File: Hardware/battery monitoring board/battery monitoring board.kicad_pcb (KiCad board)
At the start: 2 copper layers, 142 x 53.3 mm, 71 parts, among them J1 Conn_01x02, J10 Conn_01x02, J2 Conn_01x02, J3 S5B-XH-A, J4 Conn_01x02, J5 Conn_01x02, J6 Conn_01x02, J7 Conn_01x02, J8 Conn_01x02, J9 S5B-XH-A, K1 Relay_SPST-NO, Q1 PNP, Q2 PN2222A, U1 MAX31855KASA

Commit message: rearranged parts
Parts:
- moved J4 56.4 mm to (138.4, 61.6), turned to 90 degrees
- moved J3 48.6 mm to (145.7, 47.3), turned to 90 degrees
- moved J9 45.3 mm to (145.4, 30.5), turned to 90 degrees
- moved FB2 42.6 mm to (130.8, 67.7), turned to 180 degrees
- moved TP4 38.6 mm to (132.1, 61.6), turned to 0 degrees
- moved FB1 37.9 mm to (132.1, 60.6), turned to 90 degrees
- moved TP5 37.3 mm to (132.1, 59.6), turned to 0 degrees
- moved R3 35.6 mm to (135.8, 41.3), turned to -90 degrees
- moved TP6 32.1 mm to (128.6, 61.6), turned to 0 degrees
- moved TP9 31.6 mm to (119.7, 70.4), turned to 0 degrees
- moved C4 31.5 mm to (128.6, 60.9), turned to -90 degrees
- moved R4 31.1 mm to (132.3, 41.3), turned to 90 degrees
- moved TP7 30.5 mm to (128.6, 59.6), turned to 0 degrees
- moved R5 29.7 mm to (135.8, 45.4), turned to 90 degrees
- moved R2 29.6 mm to (135.7, 53.6), turned to -90 degrees
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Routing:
- net /voltage monitor/OUT1: track 51.1 -> 5.37 mm
- net /voltage monitor2/OUT1: track 49.5 -> 6.77 mm
- net /voltage monitor2/OUT4: track 38.0 -> 9.09 mm
- net Net-(A1-D4): track 27.4 -> 0.00 mm, vias 1 -> 0
- net /voltage monitor2/OUT3: track 36.1 -> 9.33 mm
- net /voltage monitor/OUT3: track 34.3 -> 8.59 mm
- net /voltage monitor/OUT2: track 33.9 -> 8.69 mm
- net /voltage monitor2/OUT2: track 34.1 -> 9.13 mm
- net /voltage monitor/OUT4: track 33.5 -> 8.76 mm
- net /leak sensor/LEAK_SIGNAL: track 39.7 -> 15.9 mm
- net /e-switch/MCU_OUTPUT: track 23.8 -> 0.00 mm, vias 2 -> 0
- net +3V3: track 74.1 -> 61.0 mm, vias 1 -> 0
- net /temp sensor/cs: track 16.4 -> 26.9 mm, vias 1 -> 0
- net /temp sensor/sck: track 26.1 -> 16.5 mm, vias 1 -> 0
- net +9V: track 102.9 -> 94.0 mm
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
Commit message: updated battery board pt.II
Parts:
- removed TP4, TP5, TP6, TP7: TestPoint, Library:Test Pads
- added 1: TestPoint, PCM_4ms_TestPoint:TestPoint_Pad_06, F.Cu at (115.8, 70.1)
- added 1: TestPoint, PCM_4ms_TestPoint:TestPoint_Pad_06, F.Cu at (115.3, 56.6)
- added C1: 10nF, Capacitor_SMD:C_0805_2012Metric_Pad1.18x1.45mm_HandSolder, F.Cu at (122.2, 74.2)
- added C8: 10nF, Capacitor_SMD:C_0805_2012Metric_Pad1.18x1.45mm_HandSolder, F.Cu at (121.9, 57.4)
- added D2: Green LED, Diode_SMD:D_0805_2012Metric_Pad1.15x1.40mm_HandSolder, F.Cu at (98.5, 43.4)
- added D8: LED, Diode_SMD:D_0805_2012Metric_Pad1.15x1.40mm_HandSolder, F.Cu at (138.4, 70.4)
- added R18: 360, Resistor_SMD:R_0805_2012Metric_Pad1.20x1.40mm_HandSolder, F.Cu at (141.5, 70.4)
- added R2: 150, Resistor_SMD:R_0805_2012Metric_Pad1.20x1.40mm_HandSolder, F.Cu at (103.4, 43.4)
- added U1: MCP3008, PCM_Package_SO_AKL:SOIC-16_3.9x9.9mm_P1.27mm, F.Cu at (109.9, 56.1)
- 2: renamed from TP16; footprint Library:Test Pads -> PCM_4ms_TestPoint:TestPoint_Pad_06
- 2: renamed from TP3; footprint Library:Test Pads -> PCM_4ms_TestPoint:TestPoint_Pad_06
- 3: renamed from TP15; footprint Library:Test Pads -> PCM_4ms_TestPoint:TestPoint_Pad_06
- 3: renamed from TP2; footprint Library:Test Pads -> PCM_4ms_TestPoint:TestPoint_Pad_06
- 4: renamed from TP14; footprint Library:Test Pads -> PCM_4ms_TestPoint:TestPoint_Pad_06
- 4: renamed from TP1; footprint Library:Test Pads -> PCM_4ms_TestPoint:TestPoint_Pad_06
- D7: renamed from D5; footprint Diode_SMD:D_0805_2012Metric_Pad1.15x1.40mm_HandSolder -> Diode_SMD:D_SMA
- J3, J9: footprint Library:JST_S5B-XH-A -> Connector_JST:JST_XH_B5B-XH-A_1x05_P2.50mm_Vertical
- J9: renamed from J10; footprint Library:JST_BM02B-GHS-TBT_LF__SN_ -> Library:DEANS
- Leak: renamed from TP11; footprint Library:Test Pads -> PCM_4ms_TestPoint:TestPoint_Pad_06; moved to F.Cu
- R1: value 147 -> 150
- R21: renamed from R22; value 11.5k -> 20.5k
- R24: renamed from R21; value 16.5k -> 11.5k
- R25: renamed from R18; value 19.6k -> 23.2k
- R5: renamed from R7; value 11.5k -> 20.5k
- R8: renamed from R6; value 16.5k -> 11.5k
- R9: renamed from R3; value 19.6k -> 23.2k
- TP10: renamed from TP9; footprint Library:Test Pads -> PCM_4ms_TestPoint:TestPoint_Pad_06
- TP13: renamed from TP12; footprint Library:Test Pads -> PCM_4ms_TestPoint:TestPoint_Pad_06; moved to F.Cu
- TP14: renamed from TP13; footprint Library:Test Pads -> PCM_4ms_TestPoint:TestPoint_Pad_06; moved to F.Cu
- TP9: renamed from TP8; footprint Library:Test Pads -> PCM_4ms_TestPoint:TestPoint_Pad_06; moved to F.Cu
- sck: renamed from TP10; footprint Library:Test Pads -> PCM_4ms_TestPoint:TestPoint_Pad_06
- moved R13 64.8 mm to (82.3, 85.9), turned to 90 degrees
- moved R14 64.0 mm to (83.1, 82.3), turned to 180 degrees
- moved Q1 63.9 mm to (82.8, 76.5)
- moved R15 63.9 mm to (82.8, 72.4)
- moved R16 63.9 mm to (82.8, 68.8)
- moved D6 63.8 mm to (82.8, 65.5)
- moved Leak 59.9 mm to (84.8, 62.2), turned to 0 degrees
- moved R1 51.8 mm to (88.1, 43.4), turned to 0 degrees
- moved C7 47.4 mm to (82.0, 90.4)
- moved TP9 41.3 mm to (111.0, 97.5), turned to 180 degrees
- moved D1 40.9 mm to (93.2, 43.4), turned to 0 degrees
- moved sck 36.2 mm to (103.6, 98.3)
- moved D4 29.4 mm to (109.0, 82.3), turned to 0 degrees
- moved J3 29.1 mm to (130.6, 72.2)
- moved J9 29.1 mm to (130.5, 55.5)
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- renumbered C8 to C10, C7 to C11, C3 to C2, C2 to C3, C1 to C4, C4 to C5, C5 to C6, C6 to C7, D2 to D4, D3 to D5, D4 to D6, R4 to R10, R9 to R11, R10 to R12, R11 to R13, R12 to R14, R13 to R15, R14 to R16, R15 to R17, R16 to R19, R17 to R20, R23 to R22, R20 to R23, R19 to R26, R2 to R4, R8 to R6, R5 to R7, U1 to U2
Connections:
- 2 pad 1: /voltage monitor2/OUT4 -> /voltage monitor2/OUT2
- 2 pad 1: /voltage monitor/OUT4 -> /voltage monitor/OUT2
- 4 pad 1: /voltage monitor2/OUT2 -> /voltage monitor2/OUT4
- 4 pad 1: /voltage monitor/OUT2 -> /voltage monitor/OUT4
- A1 pad 12: unconnected-(A1-D9-Pad12) -> Net-(A1-D9)
- A1 pad 14: unconnected-(A1-D11-Pad14) -> Net-(A1-D11)
- A1 pad 19: /voltage monitor/OUT1 -> unconnected-(A1-A0-Pad19)
- A1 pad 20: /voltage monitor/OUT2 -> unconnected-(A1-A1-Pad20)
- A1 pad 21: /voltage monitor/OUT3 -> unconnected-(A1-A2-Pad21)
- A1 pad 22: /voltage monitor/OUT4 -> unconnected-(A1-A3-Pad22)
- A1 pad 23: /voltage monitor2/OUT1 -> unconnected-(A1-A4-Pad23)
- A1 pad 24: /voltage monitor2/OUT2 -> unconnected-(A1-A5-Pad24)
- A1 pad 25: /voltage monitor2/OUT3 -> unconnected-(A1-A6-Pad25)
- A1 pad 26: /voltage monitor2/OUT4 -> unconnected-(A1-A7-Pad26)
- A1 pad 8: unconnected-(A1-D5-Pad8) -> Net-(A1-D5)
- C11 pad 1: /voltage monitor2/OUT2 -> /voltage monitor2/OUT4
- C2 pad 1: /voltage monitor/OUT4 -> /voltage monitor/OUT2
- C4 pad 1: /voltage monitor/OUT2 -> /voltage monitor/OUT4
- C9 pad 1: /voltage monitor2/OUT4 -> /voltage monitor2/OUT2
- Q1 pad 1: Net-(Q1-B) -> /leak sensor/LEAK_SIGNAL
- Q1 pad 2: +3V3 -> Net-(Q1-B)
- Q1 pad 3: /leak sensor/LEAK_SIGNAL -> +3V3
- R10 pad 2: /voltage monitor/OUT2 -> /voltage monitor/OUT4
- R21 pad 1: /voltage monitor2/OUT4 -> /voltage monitor2/OUT2
- R22 pad 1: /voltage monitor2/OUT4 -> /voltage monitor2/OUT2
- R25 pad 1: /voltage monitor2/OUT2 -> /voltage monitor2/OUT4
- R26 pad 2: /voltage monitor2/OUT2 -> /voltage monitor2/OUT4
- R5 pad 1: /voltage monitor/OUT4 -> /voltage monitor/OUT2
- R6 pad 1: /voltage monitor/OUT4 -> /voltage monitor/OUT2
- R9 pad 1: /voltage monitor/OUT2 -> /voltage monitor/OUT4
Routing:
- net /leak sensor/PROBE: track 84.4 -> 33.0 mm
- net GND: track 65.6 -> 106.8 mm, vias 117 -> 114
- net Net-(A1-D9): track 0.00 -> 33.5 mm
- net Net-(A1-D5): track 0.00 -> 27.6 mm
- net Net-(A1-D4): track 0.00 -> 23.7 mm
- net /voltage monitor/OUT1: track 5.37 -> 28.4 mm
- net +9V: track 94.0 -> 110.3 mm
- net /voltage monitor2/OUT1: track 6.77 -> 20.8 mm
- net /voltage monitor/OUT2: track 8.69 -> 20.7 mm
- net +3V3: track 61.0 -> 71.0 mm
- net /voltage monitor/OUT3: track 8.59 -> 18.3 mm
- net /voltage monitor2/OUT4: track 9.09 -> 17.9 mm
- net Net-(J4-Pin_2): track 15.3 -> 7.26 mm
- net /temp sensor/sck: track 16.5 -> 8.84 mm
- net Net-(D5-A): track 13.9 -> 7.93 mm, vias 1 -> 0
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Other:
- board size 142 x 53.3 mm -> 146.3 x 53.3 mm
- board text added: "Battery Monitoring Board v2 4/12/2024"
- board text removed: "Battery Monitoring Board v1 12/23/2023"

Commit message: erc-clear battery board
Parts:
- added ?: , , B.Cu at (94.5, 75.7)
- added C5: 0.01u, Capacitor_SMD:C_0805_2012Metric_Pad1.18x1.45mm_HandSolder, F.Cu at (107.5, 66.8)
-  - J5 +: renamed from J5
- - J6 +: renamed from J6
- - J7 +: renamed from J7
- - J8 +: renamed from J8
- J3 -: renamed from J3
- J9: value Conn_01x02 -> - 9V BAT +
- J9 +: renamed from J9
- moved cs_t 18.7 mm to (106.7, 86.4)
- moved sck 15.8 mm to (106.7, 82.8)
- moved G*** 12.7 mm to (204.2, 90.7)
- moved so 9.88 mm to (106.7, 88.6)
- moved U1 3.31 mm to (109.7, 59.4)
- moved D5 2.29 mm to (109.5, 86.1)
- moved R12 2.29 mm to (112.3, 86.1)
- moved TP14 2.03 mm to (141.5, 77.0)
- moved 2 1.52 mm to (115.8, 67.6)
- moved D4 1.27 mm to (110.2, 82.3)
- moved R11 1.27 mm to (110.2, 78.7)
- moved 4 1.05 mm to (115.8, 61.0)
- moved 3 1.02 mm to (115.8, 64.0)
- moved C6 0.76 mm to (120.7, 80.0)
- moved U2 0.76 mm to (118.1, 85.6)
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- renumbered K1 to 9V, TP10 to cs_t, TP9 to so
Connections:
- J9 pad +: (no net) -> +9V
- J9 pad -: (no net) -> GND
- cs_t pad 1: Net-(D5-A) -> /temp sensor/cs
- sck pad 1: Net-(D4-A) -> /temp sensor/sck
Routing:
- net /e-switch/MCU_OUTPUT: track 0.00 -> 53.1 mm, vias 0 -> 1
- net /temp sensor/so: track 29.2 -> 65.8 mm, vias 0 -> 1
- net Net-(A1-D11): track 0.00 -> 33.9 mm, vias 0 -> 1
- net /temp sensor/sck: track 8.84 -> 33.7 mm, vias 0 -> 1
- net GND: track 106.8 -> 88.4 mm, vias 114 -> 117
- net +5V: track 1.27 -> 17.1 mm
- net /voltage monitor2/OUT4: track 17.9 -> 21.5 mm
- net /voltage monitor/OUT2: track 20.7 -> 17.4 mm
- net Net-(A1-D9): track 33.5 -> 30.4 mm, vias 0 -> 1
- net /voltage monitor/OUT1: track 28.4 -> 25.3 mm
- net /voltage monitor2/OUT3: track 13.9 -> 16.8 mm
- net /voltage monitor/OUT3: track 18.3 -> 15.5 mm
- net /temp sensor/cs: track 22.4 -> 24.7 mm
- net /voltage monitor2/OUT2: track 13.6 -> 15.5 mm
- net Net-(D5-A): track 7.93 -> 6.23 mm
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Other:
- board text added: "BAT_IN"
- board text added: "GND"
- board text added: "SYS_IN"
- board text added: "T+"
- board text added: "T-"
- board text added: "cs_adc"
- board text removed: "9V"

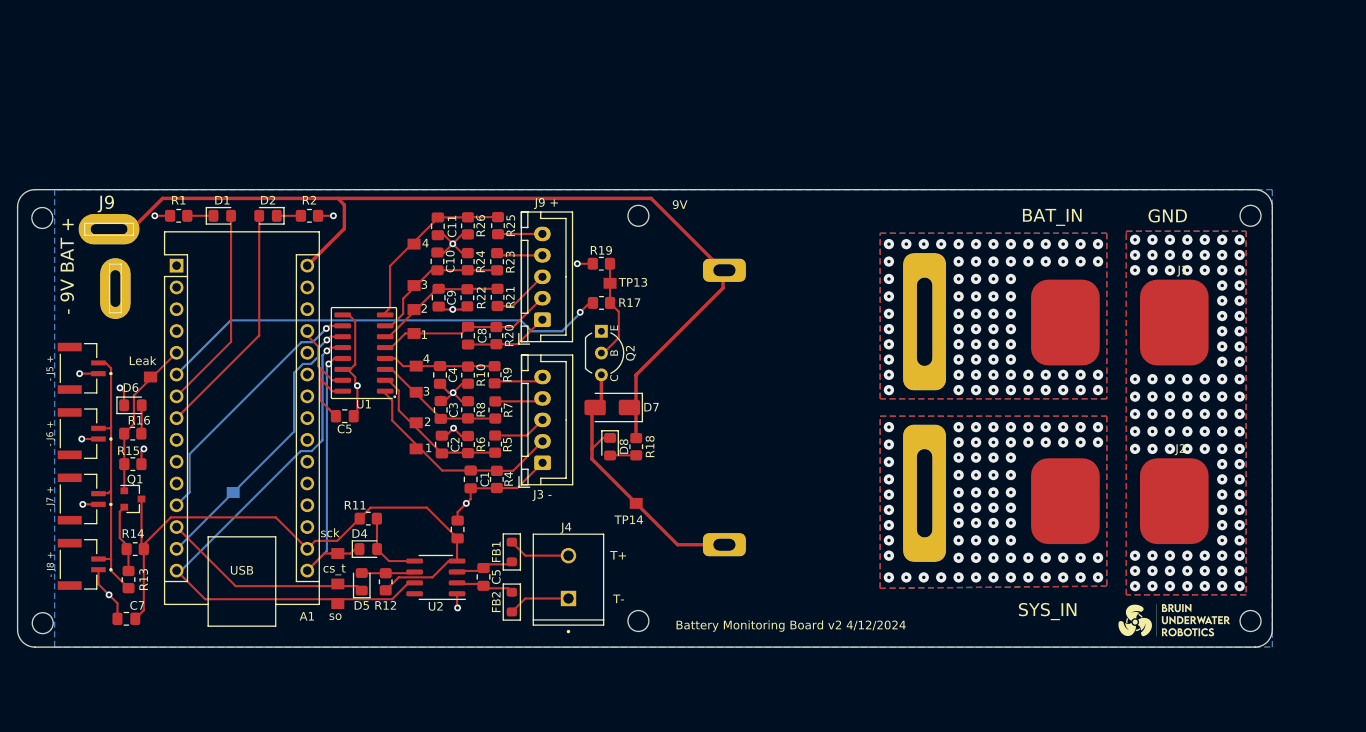
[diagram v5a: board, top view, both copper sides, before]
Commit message: updated battery pcb (voltage dividers etc)
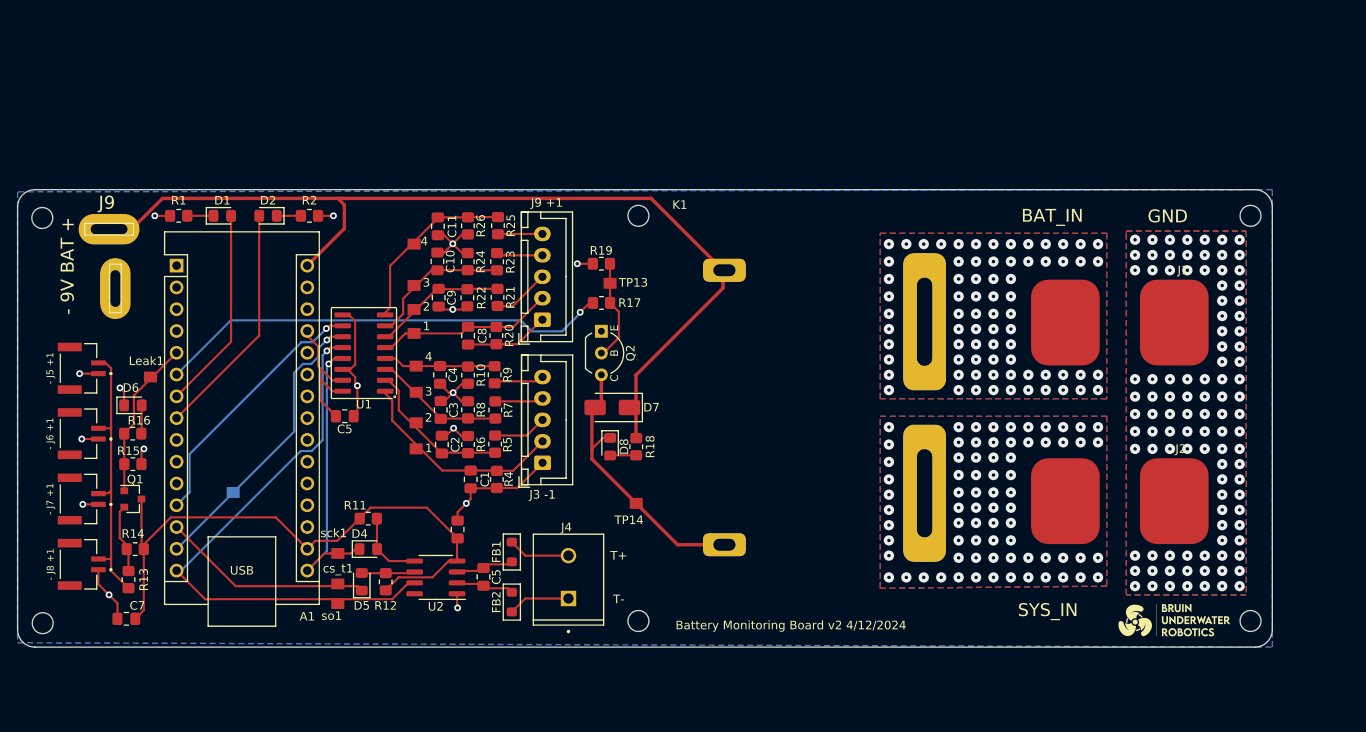
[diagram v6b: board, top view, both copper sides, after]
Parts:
-  - J5 +1: renamed from  - J5 +
- - J6 +1: renamed from - J6 +
- - J7 +1: renamed from - J7 +
- - J8 +1: renamed from - J8 +
- J3 -1: renamed from J3 -
- J9 +1: renamed from J9 +
- R20, R4: value 10k -> 20k
- R21, R5: value 20.5k -> 10k
- R22, R6: value 23.2k -> 10k
- R23, R7: value 20.5k -> 20k
- R24, R8: value 11.5k -> 10k
- R25, R9: value 23.2k -> 30k
- renumbered 1 to 11, 1 to 12, 2 to 21, 3 to 31, 3 to 32, 4 to 41, 4 to 42, 9V to K1, Leak to Leak1, cs_t to cs_t1, sck to sck1, so to so1
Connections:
- J9 pad +: +9V -> (no net)
- J9 pad -: GND -> (no net)
- cs_t1 pad 1: /temp sensor/cs -> Net-(D5-A)
- sck1 pad 1: /temp sensor/sck -> Net-(D4-A)
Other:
- board text added: "1"
- board text added: "2"
- board text added: "3"
- board text added: "4"

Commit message: finalized battery board !!
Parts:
- removed the C5 at (107.5, 66.8)
- removed J9: - 9V BAT +, Library:DEANS
- added C1: 100nF, Capacitor_SMD:C_0805_2012Metric_Pad1.18x1.45mm_HandSolder, F.Cu at (107.7, 66.5)
- added J10: - 9V BAT +, Library:DEANS, F.Cu at (80.0, 45.0)
- added R26: 10k, Resistor_SMD:R_0805_2012Metric_Pad1.20x1.40mm_HandSolder, F.Cu at (107.4, 52.3)
- moved ? 9.66 mm to (94.7, 66.0)
- moved G*** 2.03 mm to (202.2, 90.7)
- moved sck1 0.25 mm to (106.7, 83.1)
- renumbered 31 to 11V1A1, 32 to 11V1B1, 41 to 14V8A1, 42 to 14V8B1, 11 to 3V7A1, 12 to 3V7B1, 21 to 7V4A1, 2 to 7V4B1, C9 to C10, C10 to C11, C11 to C12, C1 to C2, C2 to C3, C3 to C4, C4 to C5, C5 to C6, C6 to C7, C7 to C8, C8 to C9, D5 to D3, D6 to D5, D7 to D6, D8 to D7, R12 to R10, R13 to R12, R14 to R13, R15 to R14, R16 to R15, R17 to R16, R18 to R17, R19 to R18, R20 to R19, R21 to R20, R22 to R21, R23 to R22, R24 to R23, R25 to R24, R26 to R25, R4 to R3, R5 to R4, R6 to R5, R7 to R6, R8 to R7, R9 to R8, R10 to R9, TP13 to TP1, TP14 to TP2
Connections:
- ? pad 1: Net-(A1-D11) -> Net-(A1-D9)
- D3 pad 2: Net-(D5-A) (its old number) -> Net-(D3-A)
- R10 pad 1: Net-(D5-A) (its old number) -> Net-(D3-A)
- U2 pad 6: Net-(D5-A) (its old number) -> Net-(D3-A)
- cs_t1 pad 1: Net-(D5-A) (its old number) -> /temp sensor/cs
- sck1 pad 1: Net-(D4-A) -> /temp sensor/sck
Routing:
- net Net-(D5-A) (its old number): track 6.23 -> 0.00 mm
- net Net-(D3-A): track 0.00 -> 6.23 mm
- net Net-(A1-D9): track 30.4 -> 36.3 mm
- net +5V: track 17.1 -> 22.7 mm
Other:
- outline, holes or cut-outs redrawn
- board text added: "J10"

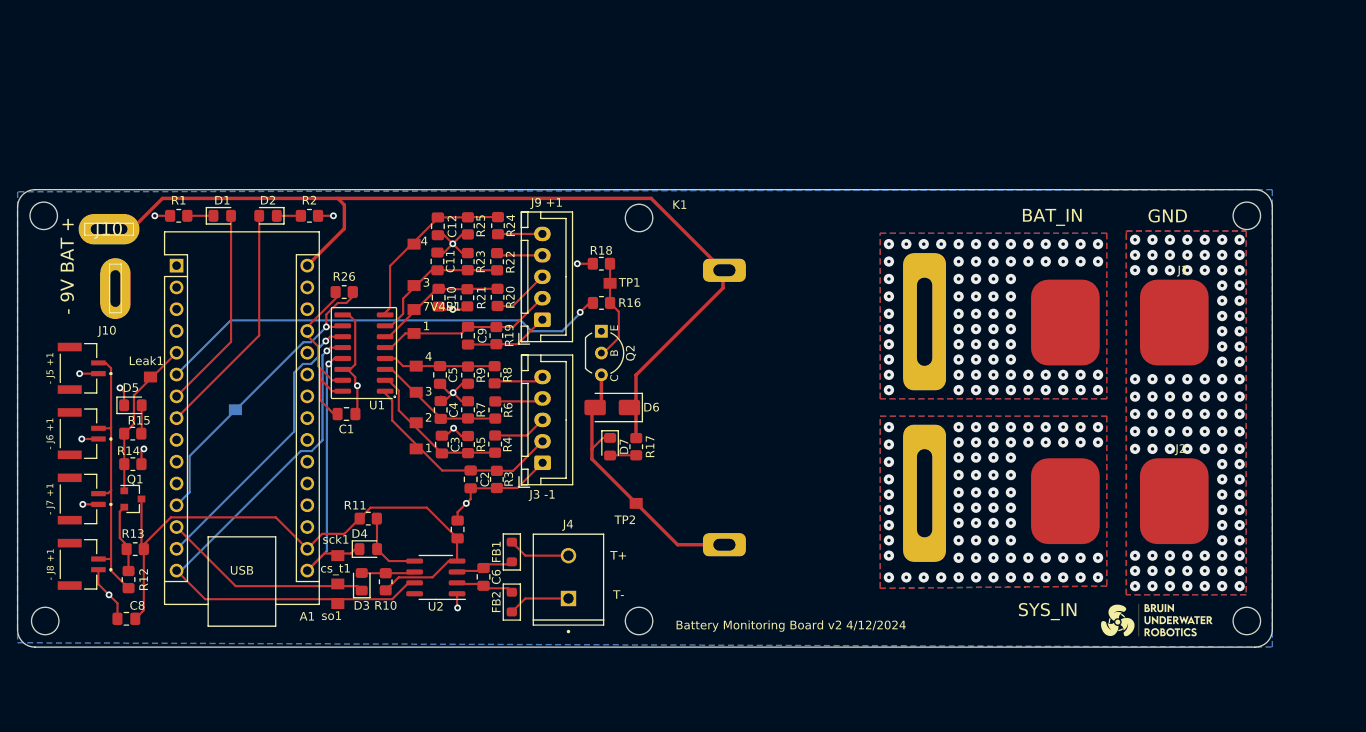
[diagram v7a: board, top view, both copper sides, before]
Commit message: resolved erc/drc issues
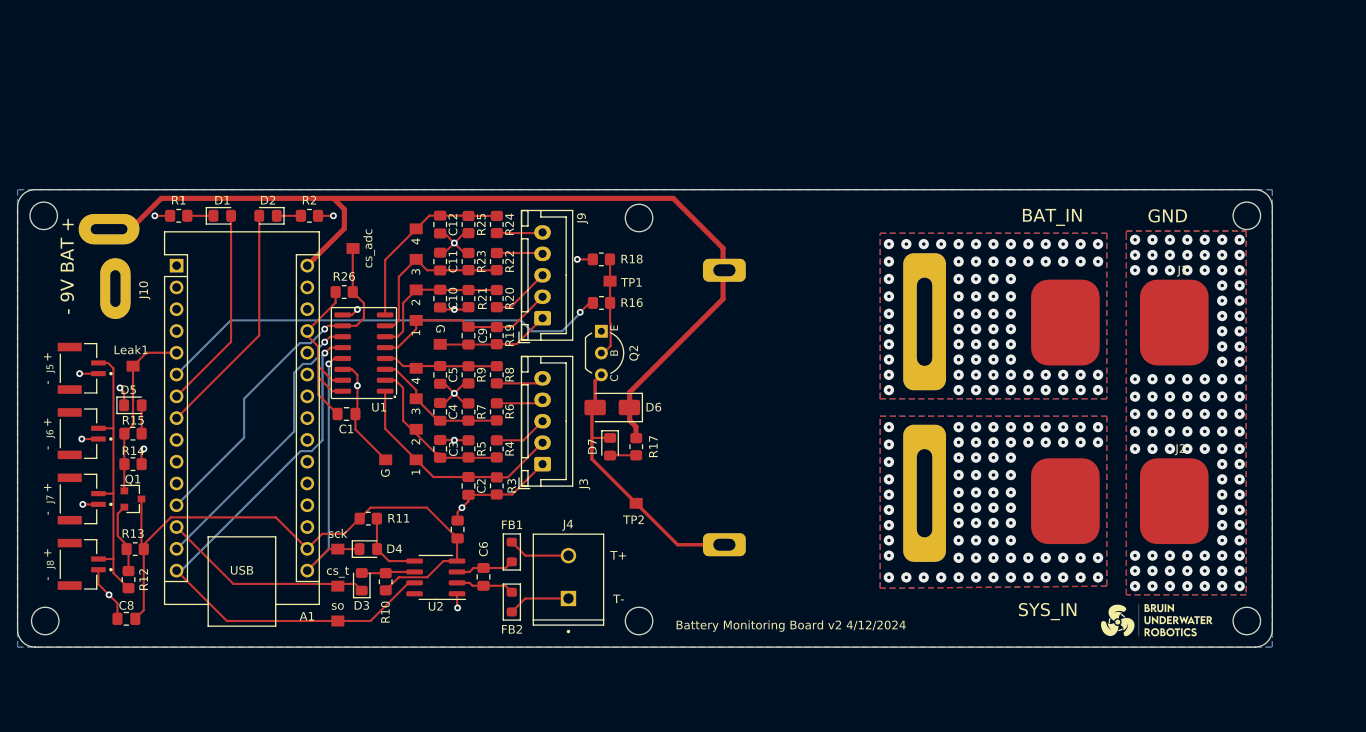
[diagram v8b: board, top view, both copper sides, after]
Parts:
- removed ?: , 
- removed J3 -1: S5B-XH-A, Connector_JST:JST_XH_B5B-XH-A_1x05_P2.50mm_Vertical
- removed J9 +1: S5B-XH-A, Connector_JST:JST_XH_B5B-XH-A_1x05_P2.50mm_Vertical
- removed cs_t1: TestPoint, PCM_4ms_TestPoint:TestPoint_Pad_06
- added J3: S5B-XH-A, Connector_JST:JST_XH_B5B-XH-A_1x05_P2.50mm_Vertical, F.Cu at (130.6, 72.4)
- added J9: S5B-XH-A, Connector_JST:JST_XH_B5B-XH-A_1x05_P2.50mm_Vertical, F.Cu at (130.6, 55.4)
- added TP4: TestPoint, PCM_4ms_TestPoint:TestPoint_Pad_06, F.Cu at (118.6, 58.4)
- added cs_adc1: TestPoint, PCM_4ms_TestPoint:TestPoint_Pad_06, F.Cu at (108.5, 47.2)
- added cs_temp1: TestPoint, PCM_4ms_TestPoint:TestPoint_Pad_06, F.Cu at (106.7, 86.6)
- added ground1: TestPoint, PCM_4ms_TestPoint:TestPoint_Pad_06, F.Cu at (112.3, 71.9)
- J5: renamed from  - J5 +1
- J6: renamed from - J6 +1
- J7: renamed from - J7 +1
- J8: renamed from - J8 +1
- moved 11V1B1 3.06 mm to (115.8, 48.5)
- moved Leak1 2.40 mm to (82.8, 61.0)
- moved 7V4B1 2.30 mm to (115.8, 52.1)
- moved so1 2.03 mm to (106.7, 90.7)
- moved 14V8B1 1.80 mm to (115.8, 45.0)
- moved 3V7B1 1.55 mm to (115.8, 55.6)
- moved 3V7A1 1.27 mm to (115.8, 71.9)
- moved C2 0.80 mm to (121.9, 74.9)
- moved 11V1A1 0.76 mm to (115.8, 64.8)
- moved 7V4A1 0.76 mm to (115.8, 68.3)
- moved R3 0.76 mm to (125.2, 74.9)
- moved sck1 0.76 mm to (106.7, 82.3)
- moved R4 0.59 mm to (125.2, 70.6)
- moved C3 0.55 mm to (118.6, 70.6)
- moved R5 0.51 mm to (121.9, 70.6)
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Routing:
- net GND: track 88.4 -> 98.0 mm, vias 117 -> 118
- net Net-(A1-D9): track 36.3 -> 42.8 mm
- net /voltage monitor2/OUT3: track 16.8 -> 19.8 mm
- net +9V: track 110.3 -> 112.6 mm
- net /temp sensor/so: track 65.8 -> 67.9 mm
- net /leak sensor/LEAK_SIGNAL: track 18.6 -> 20.7 mm
- net /voltage monitor2/OUT2: track 15.5 -> 17.2 mm
- net /voltage monitor/OUT1: track 25.3 -> 26.8 mm
- net /voltage monitor/OUT2: track 17.4 -> 18.8 mm
- net /voltage monitor2/OUT1: track 22.2 -> 23.6 mm
- net /voltage monitor/OUT3: track 15.5 -> 16.8 mm
- net +5V: track 22.7 -> 23.6 mm
- net Net-(Q2-B): track 12.0 -> 11.2 mm
- net Net-(D6-A): track 32.3 -> 33.1 mm
- net /leak sensor/PROBE: track 33.0 -> 33.7 mm
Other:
- board text added: "- +"
- board text added: "G"
- board text added: "cs_t"
- board text added: "sck"
- board text added: "so"
- board text removed: "J10"
